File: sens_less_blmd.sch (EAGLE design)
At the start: 66 parts

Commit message: 回路図を作成
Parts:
- removed CON3: (no value), user_conector:XH_4P
- removed CON4: (no value), user_conector:XH_8P
- removed IC_1: (no value), user_ic:TLP291
- removed LED2: (no value), user_leds:1608LED
- removed R_I1, R_I4, R_I5: (no value), user_rcl:R_SHUGOU
- removed R_I2, R_I3: 10k, user_rcl:R_SHUGOU2
- removed TR1, TR2, TR3, TR4, TR5, TR6: (no value), user_tr_fet_igbt:SKI03021
- removed U$1: A4919, user_ic:A4919
- removed U$10, U$11, U$12, U$13, U$8, U$9: SBR10M100P5Q, user_diode:SBR10M100P5Q
- removed U$14, U$15: ACS711, user_ic:ACS711
- removed U$2, U$3, U$4: TLP2105, user_ic:TLP2105
- removed U$5: FDC6305, user_tr_fet_igbt:FDC6305
- added C17, C8, C9: SNB, rcl:C-EUC4532
- added D1: RB160M-30TR, user_diode:SMD_DAIOD
- added D2, D3, D4, D5, D6, D7: SBR15U30SP5, user_diode:SBR15U30SP5
- added D8: SMAJ22A-13-F, user_diode:SMAJ22A-13-F
- added IC1: A4919, user_ic:A4919
- added K1, K2, K3: TLP2105, user_ic:TLP2105
- added K4: TLP291, user_ic:TLP291
- added Q1, Q2, Q3: IAUC60N04S6L045HATMA1PG-TDSON-8-57, user_tr_fet_igbt:IAUC60N04S6L045HATMA1PG-TDSON-8-57
- added Q4, Q5: AO3400A, user_tr_fet_igbt:SOT23_NFET
- added R14, R15, R19, R20, R22, R23, R24, R25, R26, R27, R28, R32, R33, R34: (no value), user_rcl:R_REG
- added R29: 3.3k, user_rcl:R_REG
- added R30: optional, user_rcl:R_REG
- added R31: 47k, user_rcl:R_REG
- added R35: OP, user_rcl:R_REG
- added U1, U2: ACS711, user_ic:ACS711
- C16: value 0.1u -> 10u
- C5, C6: value (none) -> 0.1u
- CON1: device user_conector:XH_3P -> user_conector:XH_8P
- CON2: device user_conector:XH_4P -> user_conector:XH_8P
- LED1: value (none) -> RGB_LED; device user_leds:1608LED -> user_leds:RGB_LED
- R13: value 10k -> (none)
- R18: value 10k -> 47k
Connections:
- removed net AGND: LED2.K, U$5.PIN2_S2, U$5.PIN5_S1
- removed net CURRENT_U: U$14.1_IP+, U$14.2_IP+
- removed net CURRENT_W: U$15.1_IP+, U$15.2_IP+
- removed net FAULT_O: CON1.PIN2, IC_1.4_C, R13.1
- removed net IAHI: CON4.PIN3, R_I5.2
- removed net IALO: CON4.PIN4, R_I5.1
- removed net IBHI: CON4.PIN5, R_I4.4
- removed net IBLO: CON4.PIN6, R_I4.3
- removed net ICHI: CON4.PIN7, R_I4.2
- removed net ICLO: CON4.PIN8, R_I4.1
- removed net N$27: R_I4.6, U$3.PIN1_ANODE1
- removed net N$28: R_I4.5, U$3.PIN4_ANODE2
- removed net N$29: R_I5.8, U$4.PIN1_ANODE1
- removed net N$30: R_I5.7, U$4.PIN4_ANODE2
- removed net N$35: CON2.PIN3
- removed net N$39: CON3.PIN3
- removed net U_GND: C5.2, CON2.PIN1, U$14.5_GND
- removed net U_OUT: CON2.PIN2, U$14.7_VIOUT
- removed net U_VCC: C5.1, CON2.PIN4, U$14.8_VCC
- removed net VCCIO: CON1.PIN3, R13.2
- removed net W_GND: C6.2, CON3.PIN1, U$15.5_GND
- removed net W_OUT: CON3.PIN2, U$15.7_VIOUT
- removed net W_VCC: C6.1, CON3.PIN4, U$15.8_VCC
- new net MCU_AHI: CON2.PIN2, R24.1
- new net MCU_ALO: CON2.PIN1, R23.1
- new net MCU_BHI: CON2.PIN4, R26.1
- new net MCU_BLO: CON2.PIN3, R25.1
- new net MCU_CHI: CON2.PIN6, R28.1
- new net MCU_CLO: CON2.PIN5, R27.1
- new net MCU_FAULT: CON1.PIN2, K4.3_E, R31.2
- new net MCU_POWER: CON1.PIN1, K4.4_C, R34.1
- new net N$10: IC1.PIN19_GND
- new net N$11: K1.PIN1_ANODE1, R23.2
- new net N$12: K1.PIN4_ANODE2, R24.2
- new net N$13: K2.PIN1_ANODE1, R25.2
- new net N$14: K2.PIN4_ANODE2, R26.2
- new net N$15: K3.PIN1_ANODE1, R27.2
- new net N$26: LED1.R_K, Q5.PIN2_D
- new net PHASE_U_OUT: U1.3_IP-, U1.4_IP-
- new net PHASE_W_OUT: U2.3_IP-, U2.4_IP-
- new net U_CURRENT: CON1.PIN6, U1.7_VIOUT
- new net VREF+: C5.1, C6.1, CON1.PIN4, U1.8_VCC, U2.8_VCC
- new net VREF-: C5.2, C6.2, CON1.PIN5, CON1.PIN7, U1.5_GND, U2.5_GND
- new net W_CURRENT: CON1.PIN8, U2.7_VIOUT
- net AHI: now also IC1.PIN23_AHI, K1.PIN6_VO2, R22.2; no longer R_I2.8, U$1.PIN23_AHI, U$4.PIN6_VO2
- net ALO: now also IC1.PIN24_ALO, K1.PIN7_VO1, R20.2; no longer R_I2.7, U$1.PIN24_ALO, U$4.PIN7_VO1
- net BHI: now also IC1.PIN25_BHI, K2.PIN6_VO2, R19.2; no longer R_I2.6, U$1.PIN25_BHI, U$3.PIN6_VO2
- net BLO: now also IC1.PIN26_BLO, K2.PIN7_VO1, R15.2; no longer R_I2.5, U$1.PIN26_BLO, U$3.PIN7_VO1
- net CHI: now also IC1.PIN27_CHI, K3.PIN6_VO2, R14.2; no longer R_I3.8, U$1.PIN27_CHI, U$2.PIN6_VO2
- net CLO: now also IC1.PIN28_CLO, K3.PIN7_VO1, R13.2; no longer R_I3.7, U$1.PIN28_CLO, U$2.PIN7_VO1
- net FAULT: now also IC1.PIN22_FAULT, Q4.PIN1_G, Q5.PIN1_G, R30.2, R35.2; no longer U$1.PIN22_FAULT, U$5.PIN1_G1, U$5.PIN3_G2
- net GHA: now also IC1.PIN11_GHA; no longer U$1.PIN11_GHA
- net GHB: now also IC1.PIN7_GHB; no longer U$1.PIN7_GHB
- net GHC: now also IC1.PIN3_GHC; no longer U$1.PIN3_GHC
- net GLA: now also IC1.PIN10_GLA; no longer U$1.PIN10_GLA
- net GLB: now also IC1.PIN6_GLB; no longer U$1.PIN6_GLB
- net GLC: now also IC1.PIN2_GLC; no longer U$1.PIN2_GLC
- net GND: now also C17.2, C8.2, C9.2, D3.A1, D3.A2, D5.A1, D5.A2, D7.A1, D7.A2, D8.A, IC1.PIN1_LSS, Q1.GND, Q1.GND_2, Q2.GND, Q2.GND_2, Q3.GND, Q3.GND_2; no longer TR1.PIN3_S, TR4.PIN3_S, TR6.PIN3_S, U$1.PIN1_LSS, U$10.A1, U$10.A2, U$13.A1, U$13.A2, U$9.A1, U$9.A2
- net GNDA: now also IC1.PAD, K1.PIN5_GND, K2.PIN5_GND, K3.PIN5_GND, LED1.G_K, Q4.PIN3_S, Q5.PIN3_S, R13.1, R14.1, R15.1, R19.1, R20.1, R22.1, R30.1, R35.1; no longer R_I2.1, R_I2.2, R_I2.3, R_I2.4, R_I3.1, R_I3.2, U$1.PAD, U$1.PIN19_GND, U$2.PIN5_GND, U$3.PIN5_GND, U$4.PIN5_GND
- net GNDIO: now also CON1.PIN3, CON2.PIN7, CON2.PIN8, K1.PIN2_KSODE1, K1.PIN3_KSODE2, K2.PIN2_KSODE1, K2.PIN3_KSODE2, K3.PIN2_KSODE1, K3.PIN3_KSODE2, LED1.B_K, R31.1; no longer CON1.PIN1, CON4.PIN1, IC_1.3_E, U$2.PIN2_KSODE1, U$2.PIN3_KSODE2, U$3.PIN2_KSODE1, U$3.PIN3_KSODE2, U$4.PIN2_KSODE1, U$4.PIN3_KSODE2
- net N$1: now also Q1.G_2; no longer TR2.PIN1_G
- net N$16: now also IC1.PIN13_CA; no longer U$1.PIN13_CA
- net N$17: now also IC1.PIN9_CB; no longer U$1.PIN9_CB
- net N$18: now also IC1.PIN5_CC; no longer U$1.PIN5_CC
- net N$19: now also K3.PIN4_ANODE2, R28.2; no longer LED1.K, U$5.PIN4_D2
- net N$2: now also Q1.G; no longer TR1.PIN1_G
- net N$20: now also K4.2_K, Q4.PIN2_D; no longer IC_1.2_K, U$5.PIN6_D1
- net N$21: now also C15.1, D1.C, IC1.PIN17_VBB; no longer IC_1.1_A, R_I1.4
- net N$22: now also K4.1_A, R29.2; no longer LED1.A, R_I1.3
- net N$23: now also Q2.G_2, R3.2, R9.2; no longer LED2.A, R_I1.1
- net N$24: now also LED1.G_A, R33.2; no longer R_I4.8, U$2.PIN1_ANODE1
- net N$25: now also LED1.R_A, R32.2; no longer R_I4.7, U$2.PIN4_ANODE2
- net N$3: now also Q2.G; no longer TR4.PIN1_G
- net N$4: now also LED1.B_A, R34.2; no longer R3.2, R9.2, TR3.PIN1_G
- net N$5: now also Q3.G_2; no longer TR5.PIN1_G
- net N$6: now also Q3.G; no longer TR6.PIN1_G
- net N$7: now also IC1.PIN16_CP1; no longer U$1.PIN16_CP1
- net N$8: now also IC1.PIN15_CP2; no longer U$1.PIN15_CP2
- net N$9: now also IC1.PIN14_VREG; no longer U$1.PIN14_VREG
- net PHASE_U: now also D2.A1, D2.A2, D3.K, IC1.PIN12_SA, Q1.PHASE, Q1.PHASE_2, U1.1_IP+, U1.2_IP+; no longer TR1.PIN2_D, TR2.PIN3_S, U$1.PIN12_SA, U$14.3_IP-, U$14.4_IP-, U$8.A1, U$8.A2, U$9.K
- net PHASE_V: now also D4.A1, D4.A2, D5.K, IC1.PIN8_SB, Q2.PHASE, Q2.PHASE_2; no longer TR3.PIN3_S, TR4.PIN2_D, U$1.PIN8_SB, U$10.K, U$11.A1, U$11.A2
- net PHASE_W: now also D6.A1, D6.A2, D7.K, IC1.PIN4_SC, Q3.PHASE, Q3.PHASE_2, U2.1_IP+, U2.2_IP+; no longer TR5.PIN3_S, TR6.PIN2_D, U$1.PIN4_SC, U$12.A1, U$12.A2, U$13.K, U$15.3_IP-, U$15.4_IP-
- net V5: now also IC1.PIN20_V3,V5,VDDM, K1.PIN8_VCC, K2.PIN8_VCC, K3.PIN8_VCC, R29.1, R32.1, R33.1; no longer R_I1.5, R_I1.6, R_I1.8, U$1.PIN20_V3,V5,VDDM, U$2.PIN8_VCC, U$3.PIN8_VCC, U$4.PIN8_VCC
- net VCC: now also C17.1, C8.1, C9.1, D1.A, D2.K, D4.K, D6.K, D8.C, IC1.PIN18_VBRG, Q1.BATTERY, Q1.BATTERY_2, Q2.BATTERY, Q2.BATTERY_2, Q3.BATTERY, Q3.BATTERY_2; no longer C15.1, TR2.PIN2_D, TR3.PIN2_D, TR5.PIN2_D, U$1.PIN17_VBB, U$1.PIN18_VBRG, U$11.K, U$12.K, U$8.K
- net VDSTH: now also IC1.PIN21_VDSTH; no longer U$1.PIN21_VDSTH
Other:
- note added: "25PFV330M10X10.5"
- note added: "35PFV47M6.3X6.1"
- note added: "A4919GLPTR-5-T"
- note added: "At R_{ds(on)} = 6 mohm"
- note added: "Conector"
- note added: "FaultCurrent 57 A"
- note added: "If self-turn on, add a resistor"
- note added: "Isolation Interface"
- note added: "LDO output 5V"
- note added: "MotorControlGateDriver"
- note added: "PullDown47k"
- note added: "R16 = 47k,R17 = 3.3k"
- note added: "SNB Capacitor is optional please use LowESR LowESL FilmCapacitor typicaliy [63MU105KC24532]"
- note added: "V_{dsth} = 0.34"
- note added: "V_{dsth} Range between 0.2 to 2 [V]"
- note added: "V_{dsth}= R_{2}*(Vcc-R_{1}*I_{L})/(R_{2}+R_{1})"
- note added: "typically 1k ohm must check MCU output current"
- note added: "三相フルブリッジ回路部"
- moved on the sheet: C1, C10, C11, C12, C13, C14, C15, C16, C2, C23, C3, C4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

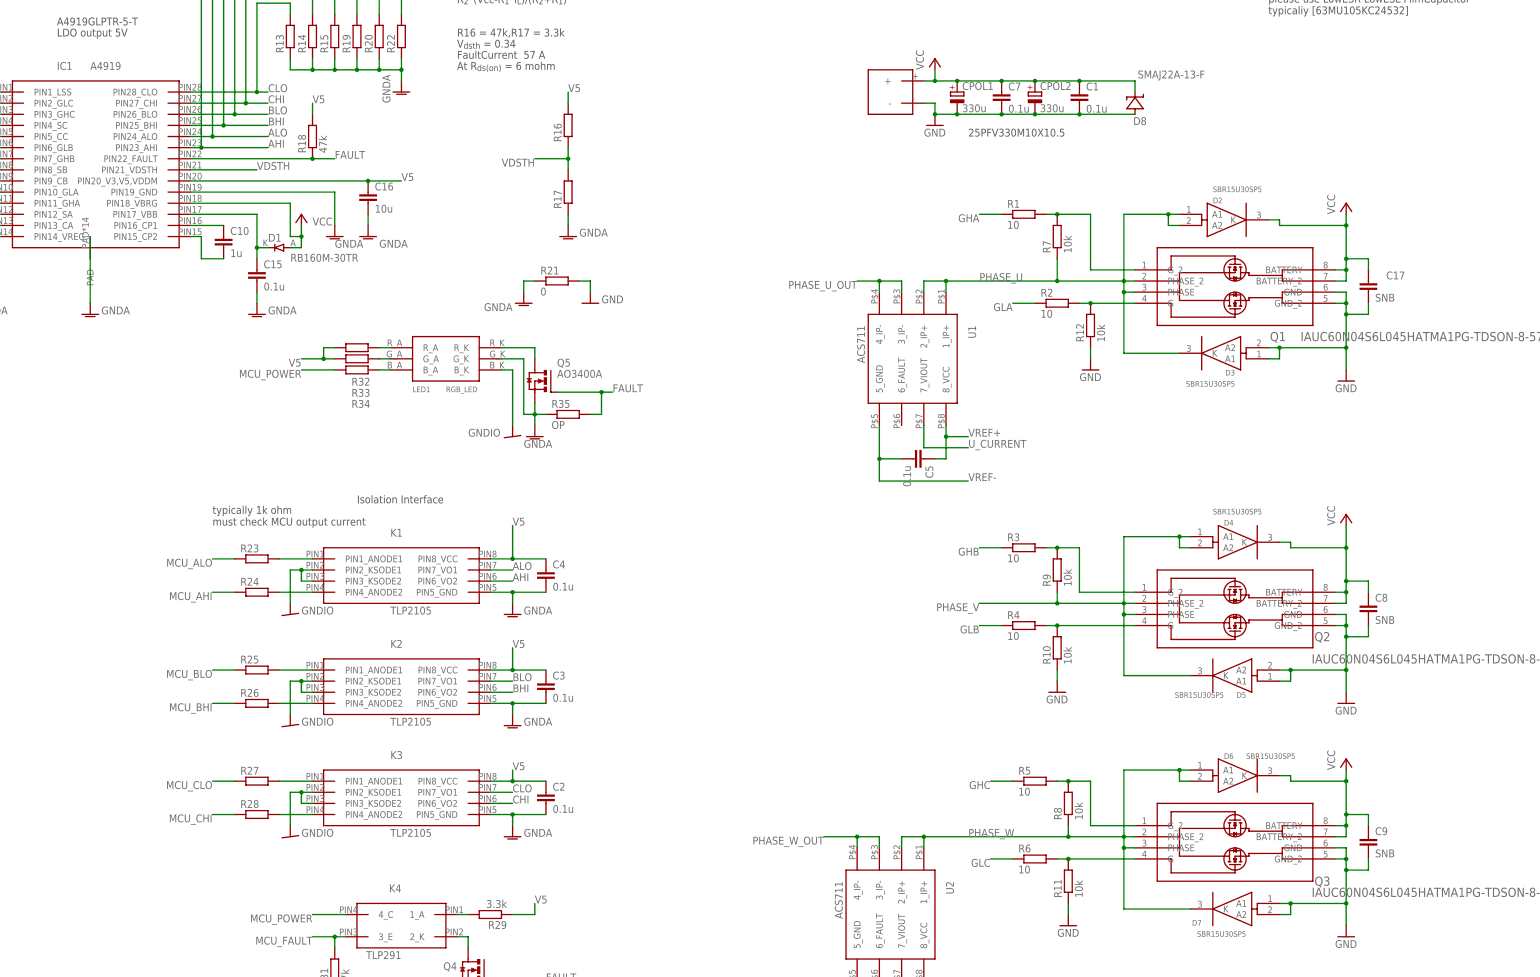
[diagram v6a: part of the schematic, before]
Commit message: fet側基板の完成とガーバーファイル追加
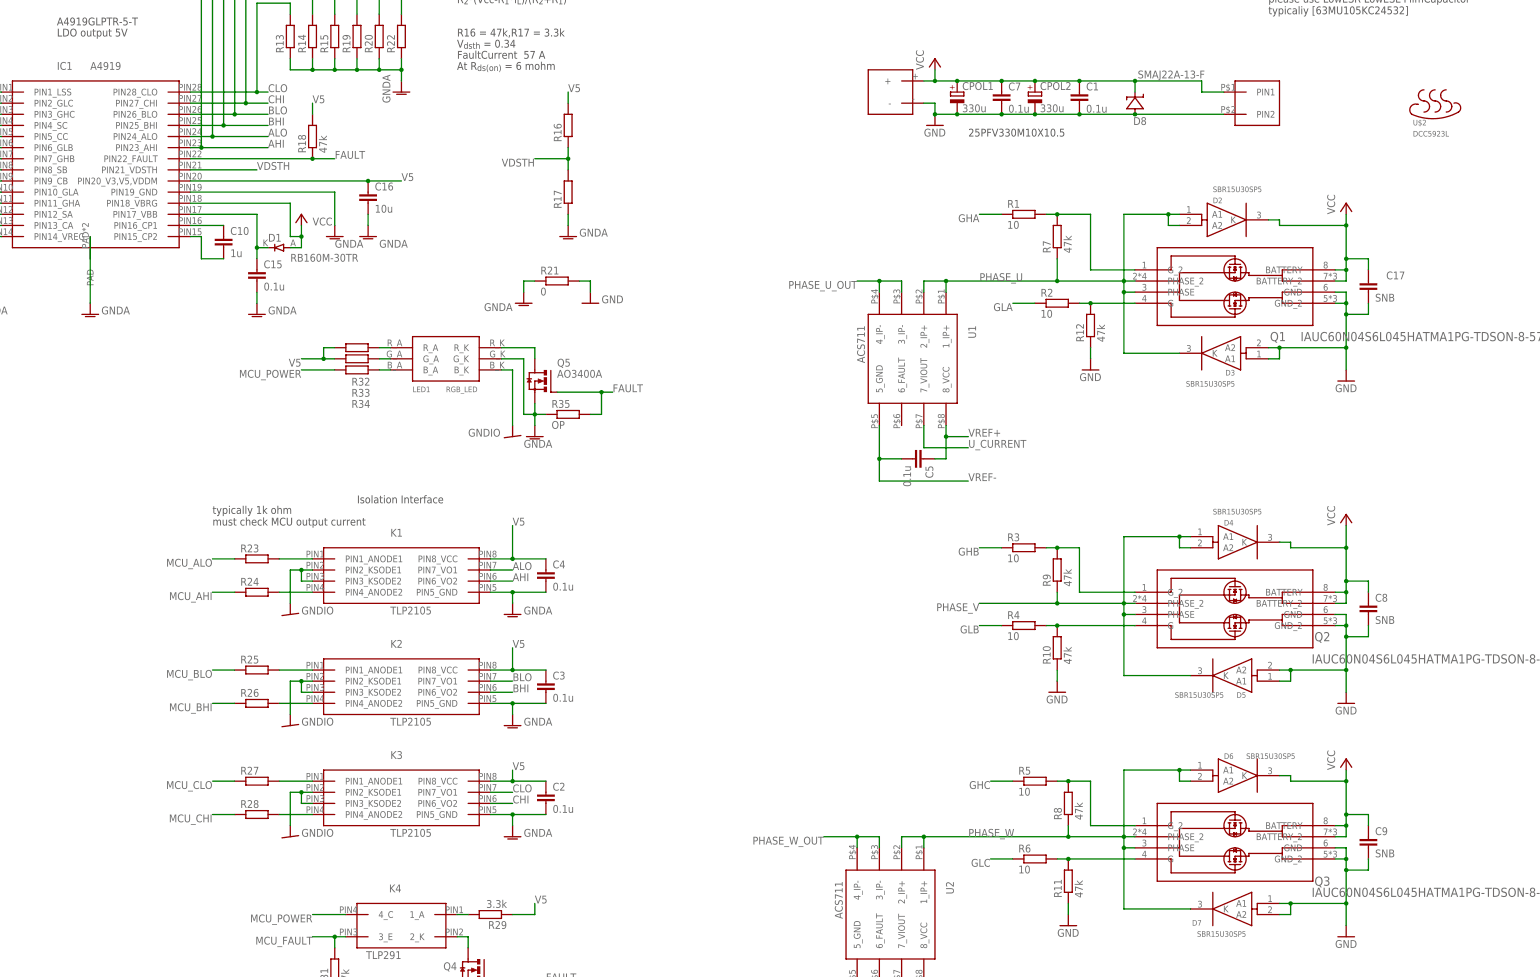
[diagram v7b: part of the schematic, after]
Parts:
- added U$1: XH_2P, user_conector:XH_2P
- added U$2: DCC5923L, user_heatshink:DCC5923L
- R10, R11, R12, R7, R8, R9: value 10k -> 47k
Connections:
- removed net N$10: IC1.PIN19_GND
- net GND: now also U$1.PIN2
- net GNDA: now also IC1.PIN19_GND
- net VCC: now also U$1.PIN1
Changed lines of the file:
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@@
 <part name="R5" library="user_rcl" deviceset="R_REG" device="" value="10"/>
 <part name="R6" library="user_rcl" deviceset="R_REG" device="" value="10"/>
-<part name="R7" library="user_rcl" deviceset="R_REG" device="" value="10k"/>
-<part name="R8" library="user_rcl" deviceset="R_REG" device="" value="10k"/>
-<part name="R9" library="user_rcl" deviceset="R_REG" device="" value="10k"/>
-<part name="R10" library="user_rcl" deviceset="R_REG" device="" value="10k"/>
-<part name="R11" library="user_rcl" deviceset="R_REG" device="" value="10k"/>
-<part name="R12" library="user_rcl" deviceset="R_REG" device="" value="10k"/>
+<part name="R7" library="user_rcl" deviceset="R_REG" device="" value="47k"/>
+<part name="R8" library="user_rcl" deviceset="R_REG" device="" value="47k"/>
+<part name="R9" library="user_rcl" deviceset="R_REG" device="" value="47k"/>
+<part name="R10" library="user_rcl" deviceset="R_REG" device="" value="47k"/>
+<part name="R11" library="user_rcl" deviceset="R_REG" device="" value="47k"/>
+<part name="R12" library="user_rcl" deviceset="R_REG" device="" value="47k"/>
 <part name="GND2" library="supply1" library_urn="urn:adsk.eagle:library:371" deviceset="GND" device=""/>
 <part name="P+1" library="supply1" library_urn="urn:adsk.eagle:library:371" deviceset="VCC" device=""/>
@@
 <part name="GND20" library="supply1" library_urn="urn:adsk.eagle:library:371" deviceset="GNDIO" device=""/>
 <part name="D8" library="user_diode" deviceset="SMAJ22A-13-F" device=""/>
+<part name="U$1" library="user_conector" deviceset="XH_2P" device=""/>
+<part name="U$2" library="user_heatshink" deviceset="DCC5923L" device=""/>
 </parts>
 <sheets>
@@
 <attribute name="VALUE" x="318.1096" y="239.3442" size="1.778" layer="96"/>
 </instance>
+<instance part="U$1" gate="G$1" x="342.9" y="233.68" smashed="yes" rot="MR0"/>
+<instance part="U$2" gate="G$1" x="386.08" y="231.14" smashed="yes">
+<attribute name="NAME" x="381" y="228.6" size="1.27" layer="95"/>
+<attribute name="VALUE" x="381" y="226.06" size="1.27" layer="96"/>
+</instance>
 </instances>
 <busses>
@@
 <wire x1="317.5" y1="231.14" x2="304.8" y2="231.14" width="0.1524" layer="91"/>
 <junction x="304.8" y="231.14"/>
+<pinref part="U$1" gate="G$1" pin="PIN2"/>
+<wire x1="337.82" y1="231.14" x2="317.5" y2="231.14" width="0.1524" layer="91"/>
+<junction x="317.5" y="231.14"/>
 </segment>
 <segment>
@@
 <pinref part="D8" gate="G$1" pin="C"/>
 <wire x1="317.5" y1="238.76" x2="317.5" y2="236.22" width="0.1524" layer="91"/>
+<wire x1="317.5" y1="238.76" x2="332.74" y2="238.76" width="0.1524" layer="91"/>
+<wire x1="332.74" y1="238.76" x2="332.74" y2="236.22" width="0.1524" layer="91"/>
+<junction x="317.5" y="238.76"/>
+<pinref part="U$1" gate="G$1" pin="PIN1"/>
+<wire x1="332.74" y1="236.22" x2="337.82" y2="236.22" width="0.1524" layer="91"/>
 </segment>
 <segment>
@@
 <wire x1="177.8" y1="162.56" x2="180.34" y2="162.56" width="0.1524" layer="91"/>
 </segment>
+<segment>
+<pinref part="IC1" gate="G$1" pin="PIN19_GND"/>
+<wire x1="101.6" y1="213.36" x2="134.62" y2="213.36" width="0.1524" layer="91"/>
+<pinref part="GND4" gate="1" pin="GNDA"/>
+<wire x1="134.62" y1="213.36" x2="134.62" y2="205.74" width="0.1524" layer="91"/>
+</segment>
 </net>
 <net name="N$7" class="0">
@@
 </segment>
 </net>
-<net name="N$10" class="0">
-<segment>
-<wire x1="101.6" y1="213.36" x2="134.62" y2="213.36" width="0.1524" layer="91"/>
-<pinref part="GND4" gate="1" pin="GNDA"/>
-<wire x1="134.62" y1="213.36" x2="134.62" y2="205.74" width="0.1524" layer="91"/>
-<pinref part="IC1" gate="G$1" pin="PIN19_GND"/>
-</segment>
-</net>
